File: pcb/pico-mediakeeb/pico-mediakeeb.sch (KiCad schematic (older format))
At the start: 8 parts

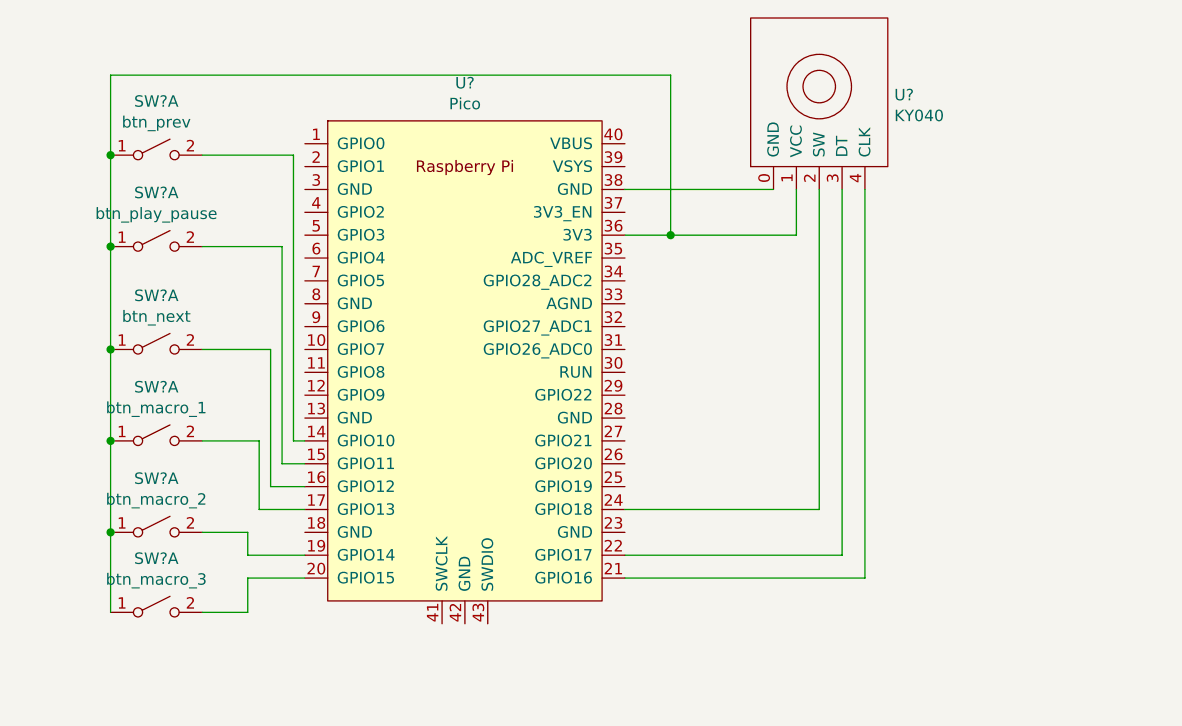
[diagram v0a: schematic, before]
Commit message: Make labels more readable
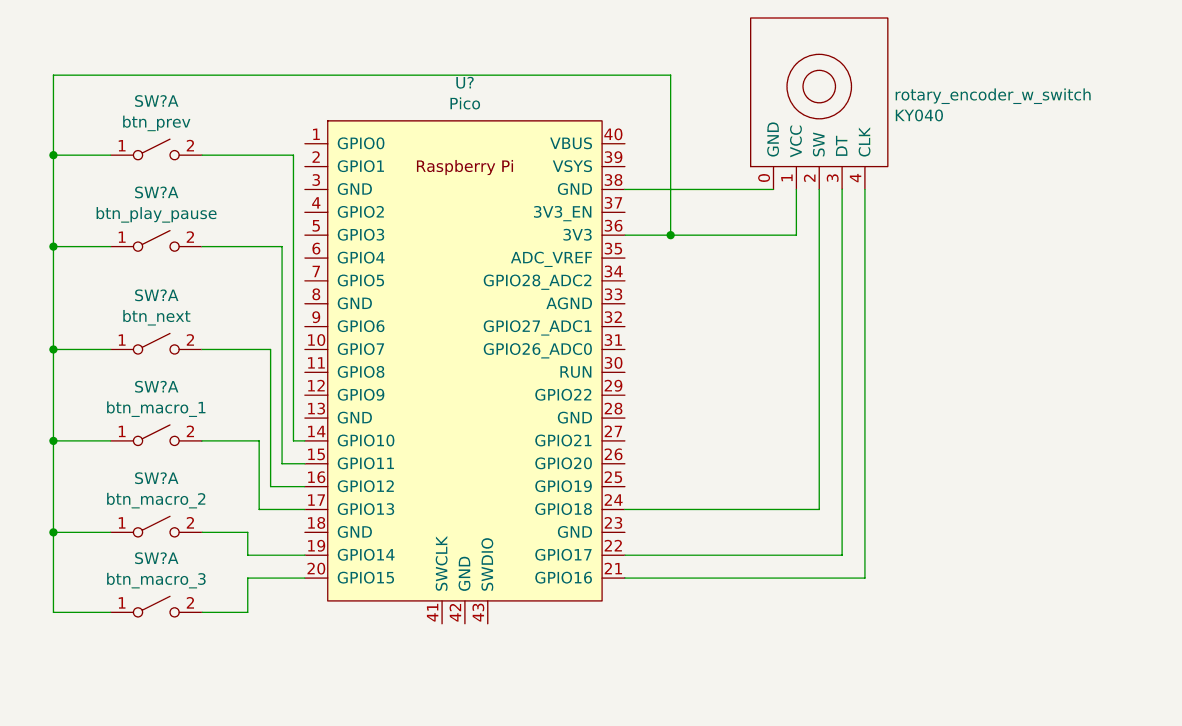
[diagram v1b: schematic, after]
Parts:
- gave numbers to parts that had none: 1
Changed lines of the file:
@@
 	4950 1650 4950 950
-Wire Wire Line
-	4950 950  2500 950
-Wire Wire Line
-	2500 950  2500 1300
-Connection ~ 2500 1300
-Wire Wire Line
-	2500 1300 2500 1700
-Connection ~ 2500 1700
-Wire Wire Line
-	2500 1700 2500 2150
-Connection ~ 2500 2150
-Wire Wire Line
-	2500 2150 2500 2550
-Connection ~ 2500 2550
-Wire Wire Line
-	2500 2550 2500 2950
-Connection ~ 2500 2950
-Wire Wire Line
-	2500 2950 2500 3300
-$Comp
-L pico-mediakeeb:KY040 U?
-U 1 1 6096AC9D
-P 5600 1000
-F 0 "U?" H 5928 963 50  0000 L CNN
-F 1 "KY040" H 5928 872 50  0000 L CNN
-F 2 "" H 5600 1000 50  0001 C CNN
-F 3 "" H 5600 1000 50  0001 C CNN
-	1    5600 1000
-	1    0    0    -1
-$EndComp
 Wire Wire Line
 	4750 1450 5400 1450
@@
 Wire Wire Line
 	5800 3150 4750 3150
+$Comp
+L pico-mediakeeb:KY040 rotary_encoder_w_switch
+U 1 1 6096AC9D
+P 5600 1000
+F 0 "rotary_encoder_w_switch" H 5928 963 50  0000 L CNN
+F 1 "KY040" H 5928 872 50  0000 L CNN
+F 2 "" H 5600 1000 50  0001 C CNN
+F 3 "" H 5600 1000 50  0001 C CNN
+	1    5600 1000
+	1    0    0    -1
+$EndComp
+Wire Wire Line
+	2500 3300 2250 3300
+Wire Wire Line
+	2250 3300 2250 2950
+Wire Wire Line
+	2250 950  4950 950
+Wire Wire Line
+	2500 1300 2250 1300
+Connection ~ 2250 1300
+Wire Wire Line
+	2250 1300 2250 950
+Wire Wire Line
+	2500 1700 2250 1700
+Connection ~ 2250 1700
+Wire Wire Line
+	2250 1700 2250 1300
+Wire Wire Line
+	2500 2150 2250 2150
+Connection ~ 2250 2150
+Wire Wire Line
+	2250 2150 2250 1700
+Wire Wire Line
+	2500 2550 2250 2550
+Connection ~ 2250 2550
+Wire Wire Line
+	2250 2550 2250 2150
+Wire Wire Line
+	2500 2950 2250 2950
+Connection ~ 2250 2950
+Wire Wire Line
+	2250 2950 2250 2550
 $EndSCHEMATC

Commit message: Update schematic to use generic rotary encoder
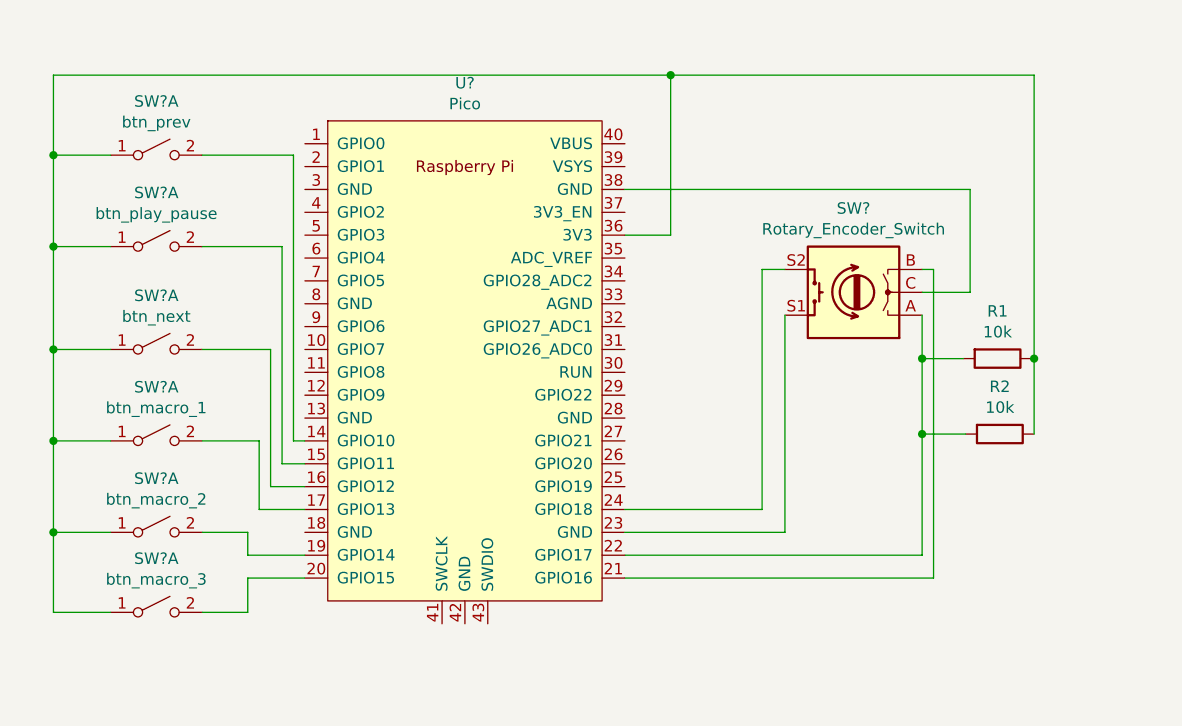
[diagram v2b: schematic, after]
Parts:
- removed rotary_encoder_w_switch: KY040, symbol pico-mediakeeb:KY040
- added R1, R2: 10k, symbol Device:R
- added SW?: Rotary_Encoder_Switch, symbol Device:Rotary_Encoder_Switch
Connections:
- net at U?.21 (GPIO16): now also SW?.B
- net at U?.22 (GPIO17): now also R1.2, R2.2, SW?.A
- net at U?.23 (GND): now also SW?.S1
- net at U?.24 (GPIO18): now also SW?.S2
- net at SW?.1 (A), SW?.1 (A), SW?.1 (A)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: now also R1.1, R2.1
- net at U?.38 (GND): now also SW?.C
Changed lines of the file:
@@
 	4950 1650 4950 950
-Wire Wire Line
-	4750 1450 5400 1450
-Wire Wire Line
-	5500 1450 5500 1650
-Wire Wire Line
-	5500 1650 4950 1650
-Connection ~ 4950 1650
-Wire Wire Line
-	5600 1450 5600 2850
-Wire Wire Line
-	5600 2850 4750 2850
-Wire Wire Line
-	5700 1450 5700 3050
-Wire Wire Line
-	5700 3050 4750 3050
-Wire Wire Line
-	5800 1450 5800 3150
-Wire Wire Line
-	5800 3150 4750 3150
-$Comp
-L pico-mediakeeb:KY040 rotary_encoder_w_switch
-U 1 1 6096AC9D
-P 5600 1000
-F 0 "rotary_encoder_w_switch" H 5928 963 50  0000 L CNN
-F 1 "KY040" H 5928 872 50  0000 L CNN
-F 2 "" H 5600 1000 50  0001 C CNN
-F 3 "" H 5600 1000 50  0001 C CNN
-	1    5600 1000
-	1    0    0    -1
-$EndComp
 Wire Wire Line
 	2500 3300 2250 3300
@@
 Wire Wire Line
 	2250 2950 2250 2550
+$Comp
+L Device:Rotary_Encoder_Switch SW?
+U 1 1 6097F51C
+P 5750 1900
+F 0 "SW?" H 5750 1533 50  0000 C CNN
+F 1 "Rotary_Encoder_Switch" H 5750 1624 50  0000 C CNN
+F 2 "" H 5600 2060 50  0001 C CNN
+F 3 "~" H 5750 2160 50  0001 C CNN
+	1    5750 1900
+	-1   0    0    1
+$EndComp
+Wire Wire Line
+	6050 2000 6050 2190
+Wire Wire Line
+	6050 3050 4750 3050
+Wire Wire Line
+	6050 1800 6100 1800
+Wire Wire Line
+	6100 1800 6100 3150
+Wire Wire Line
+	6100 3150 4750 3150
+Wire Wire Line
+	4750 2950 5450 2950
+Wire Wire Line
+	5450 2950 5450 2000
+Wire Wire Line
+	5450 1800 5350 1800
+Wire Wire Line
+	5350 1800 5350 2850
+Wire Wire Line
+	5350 2850 4750 2850
+Wire Wire Line
+	6050 1900 6260 1900
+Wire Wire Line
+	6260 1900 6260 1450
+Wire Wire Line
+	6260 1450 4750 1450
+$Comp
+L Device:R R1
+U 1 1 6099BEDA
+P 6380 2190
+F 0 "R1" V 6173 2190 50  0000 C CNN
+F 1 "10k" V 6264 2190 50  0000 C CNN
+F 2 "" V 6310 2190 50  0001 C CNN
+F 3 "~" H 6380 2190 50  0001 C CNN
+	1    6380 2190
+	0    1    1    0
+$EndComp
+$Comp
+L Device:R R2
+U 1 1 6099D114
+P 6390 2520
+F 0 "R2" V 6183 2520 50  0000 C CNN
+F 1 "10k" V 6274 2520 50  0000 C CNN
+F 2 "" V 6320 2520 50  0001 C CNN
+F 3 "~" H 6390 2520 50  0001 C CNN
+	1    6390 2520
+	0    1    1    0
+$EndComp
+Wire Wire Line
+	6050 2190 6230 2190
+Connection ~ 6050 2190
+Wire Wire Line
+	6050 2190 6050 2520
+Wire Wire Line
+	6050 2520 6240 2520
+Connection ~ 6050 2520
+Wire Wire Line
+	6050 2520 6050 3050
+Wire Wire Line
+	6540 2520 6540 2190
+Wire Wire Line
+	6540 2190 6530 2190
+Wire Wire Line
+	6540 2190 6540 950
+Wire Wire Line
+	6540 950  4950 950
+Connection ~ 6540 2190
+Connection ~ 4950 950
 $EndSCHEMATC

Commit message: Update schematic
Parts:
- R1, R2: footprint (none) -> Resistor_THT:R_Axial_DIN0204_L3.6mm_D1.6mm_P5.08mm_Vertical
- SW1, SW2, SW3, SW4, SW5, SW6: renamed from SW?; footprint (none) -> Button_Switch_Keyboard:SW_Cherry_MX_1.00u_Plate
- SW7: renamed from SW?; footprint (none) -> Rotary_Encoder:RotaryEncoder_Alps_EC11E-Switch_Vertical_H20mm
- U1: renamed from U?; footprint RPi_Pico:RPi_Pico_SMD_TH -> Raspberry:RPi_Pico_SMD_TH
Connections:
- no-connect marks 0 -> 31
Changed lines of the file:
@@
 $EndDescr
 $Comp
-L MCU_RaspberryPi_and_Boards:Pico U?
+L MCU_RaspberryPi_and_Boards:Pico U1
 U 1 1 609308D7
 P 4050 2200
-F 0 "U?" H 4050 3415 50  0000 C CNN
+F 0 "U1" H 4050 3415 50  0000 C CNN
 F 1 "Pico" H 4050 3324 50  0000 C CNN
-F 2 "RPi_Pico:RPi_Pico_SMD_TH" V 4050 2200 50  0001 C CNN
+F 2 "Raspberry:RPi_Pico_SMD_TH" V 4050 2200 50  0001 C CNN
 F 3 "" H 4050 2200 50  0001 C CNN
 	1    4050 2200
 	1    0    0    -1
 $EndComp
-$Comp
-L Switch:SW_DPST_x2 SW?
-U 1 1 60931FB6
-P 2700 1300
-F 0 "SW?" H 2700 1535 50  0000 C CNN
-F 1 "btn_prev" H 2700 1444 50  0000 C CNN
-F 2 "" H 2700 1300 50  0001 C CNN
-F 3 "~" H 2700 1300 50  0001 C CNN
-	1    2700 1300
-	1    0    0    -1
-$EndComp
-$Comp
-L Switch:SW_DPST_x2 SW?
-U 1 1 6093271C
-P 2700 1700
-F 0 "SW?" H 2700 1935 50  0000 C CNN
-F 1 "btn_play_pause" H 2700 1844 50  0000 C CNN
-F 2 "" H 2700 1700 50  0001 C CNN
-F 3 "~" H 2700 1700 50  0001 C CNN
-	1    2700 1700
-	1    0    0    -1
-$EndComp
-$Comp
-L Switch:SW_DPST_x2 SW?
-U 1 1 609327D9
-P 2700 2150
-F 0 "SW?" H 2700 2385 50  0000 C CNN
-F 1 "btn_next" H 2700 2294 50  0000 C CNN
-F 2 "" H 2700 2150 50  0001 C CNN
-F 3 "~" H 2700 2150 50  0001 C CNN
-	1    2700 2150
-	1    0    0    -1
-$EndComp
-$Comp
-L Switch:SW_DPST_x2 SW?
-U 1 1 60940915
-P 2700 2550
-F 0 "SW?" H 2700 2785 50  0000 C CNN
-F 1 "btn_macro_1" H 2700 2694 50  0000 C CNN
-F 2 "" H 2700 2550 50  0001 C CNN
-F 3 "~" H 2700 2550 50  0001 C CNN
-	1    2700 2550
-	1    0    0    -1
-$EndComp
-$Comp
-L Switch:SW_DPST_x2 SW?
-U 1 1 6094091B
-P 2700 2950
-F 0 "SW?" H 2700 3185 50  0000 C CNN
-F 1 "btn_macro_2" H 2700 3094 50  0000 C CNN
-F 2 "" H 2700 2950 50  0001 C CNN
-F 3 "~" H 2700 2950 50  0001 C CNN
-	1    2700 2950
-	1    0    0    -1
-$EndComp
-$Comp
-L Switch:SW_DPST_x2 SW?
-U 1 1 60940921
-P 2700 3300
-F 0 "SW?" H 2700 3535 50  0000 C CNN
-F 1 "btn_macro_3" H 2700 3444 50  0000 C CNN
-F 2 "" H 2700 3300 50  0001 C CNN
-F 3 "~" H 2700 3300 50  0001 C CNN
-	1    2700 3300
-	1    0    0    -1
-$EndComp
 Wire Wire Line
 	3300 1300 3300 2550
@@
 	3300 2550 3350 2550
 Wire Wire Line
-	2900 1300 3300 1300
-Wire Wire Line
-	2900 1700 3250 1700
-Wire Wire Line
 	3250 1700 3250 2650
 Wire Wire Line
 	3250 2650 3350 2650
 Wire Wire Line
-	2900 2150 3200 2150
-Wire Wire Line
 	3200 2150 3200 2750
 Wire Wire Line
 	3200 2750 3350 2750
 Wire Wire Line
-	2900 2550 3150 2550
-Wire Wire Line
 	3150 2550 3150 2850
 Wire Wire Line
 	3150 2850 3350 2850
 Wire Wire Line
-	2900 2950 3100 2950
-Wire Wire Line
 	3100 2950 3100 3050
 Wire Wire Line
 	3100 3050 3350 3050
-Wire Wire Line
-	2900 3300 3100 3300
 Wire Wire Line
 	3100 3300 3100 3150
@@
 	2250 2950 2250 2550
 $Comp
-L Device:Rotary_Encoder_Switch SW?
+L Device:Rotary_Encoder_Switch SW7
 U 1 1 6097F51C
 P 5750 1900
-F 0 "SW?" H 5750 1533 50  0000 C CNN
+F 0 "SW7" H 5750 1533 50  0000 C CNN
 F 1 "Rotary_Encoder_Switch" H 5750 1624 50  0000 C CNN
-F 2 "" H 5600 2060 50  0001 C CNN
+F 2 "Rotary_Encoder:RotaryEncoder_Alps_EC11E-Switch_Vertical_H20mm" H 5600 2060 50  0001 C CNN
 F 3 "~" H 5750 2160 50  0001 C CNN
 	1    5750 1900
@@
 Wire Wire Line
 	6100 3150 4750 3150
-Wire Wire Line
-	4750 2950 5450 2950
-Wire Wire Line
-	5450 2950 5450 2000
 Wire Wire Line
 	5450 1800 5350 1800
@@
 F 0 "R1" V 6173 2190 50  0000 C CNN
 F 1 "10k" V 6264 2190 50  0000 C CNN
-F 2 "" V 6310 2190 50  0001 C CNN
+F 2 "Resistor_THT:R_Axial_DIN0204_L3.6mm_D1.6mm_P5.08mm_Vertical" V 6310 2190 50  0001 C CNN
 F 3 "~" H 6380 2190 50  0001 C CNN
 	1    6380 2190
@@
 F 0 "R2" V 6183 2520 50  0000 C CNN
 F 1 "10k" V 6274 2520 50  0000 C CNN
-F 2 "" V 6320 2520 50  0001 C CNN
+F 2 "Resistor_THT:R_Axial_DIN0204_L3.6mm_D1.6mm_P5.08mm_Vertical" V 6320 2520 50  0001 C CNN
 F 3 "~" H 6390 2520 50  0001 C CNN
 	1    6390 2520
@@
 Connection ~ 6540 2190
 Connection ~ 4950 950
+NoConn ~ 4750 2050
+NoConn ~ 4750 1950
+NoConn ~ 4750 1850
+NoConn ~ 4750 1750
+NoConn ~ 4750 2750
+NoConn ~ 4750 2650
+NoConn ~ 4750 2550
+NoConn ~ 4750 2450
+NoConn ~ 4750 2350
+NoConn ~ 4750 2250
+NoConn ~ 4750 2150
+NoConn ~ 4750 1350
+NoConn ~ 4750 1250
+NoConn ~ 4750 1550
+NoConn ~ 3350 2950
+NoConn ~ 3350 2450
+NoConn ~ 3350 2350
+NoConn ~ 3350 2250
+NoConn ~ 3350 2150
+NoConn ~ 3350 2050
+NoConn ~ 3350 1950
+NoConn ~ 3350 1250
+NoConn ~ 3350 1350
+NoConn ~ 3350 1450
+NoConn ~ 3350 1550
+NoConn ~ 3350 1650
+NoConn ~ 3350 1750
+NoConn ~ 3350 1850
+NoConn ~ 3950 3350
+NoConn ~ 4050 3350
+NoConn ~ 4150 3350
+Wire Wire Line
+	5450 2950 5450 2000
+Wire Wire Line
+	4750 2950 5450 2950
+Wire Wire Line
+	2900 3300 3100 3300
+Wire Wire Line
+	2900 2950 3100 2950
+Wire Wire Line
+	2900 2550 3150 2550
+Wire Wire Line
+	2900 2150 3200 2150
+Wire Wire Line
+	2900 1700 3250 1700
+Wire Wire Line
+	2900 1300 3300 1300
+$Comp
+L Switch:SW_DPST_x2 SW6
+U 1 1 60940921
+P 2700 3300
+F 0 "SW6" H 2700 3535 50  0000 C CNN
+F 1 "btn_macro_3" H 2700 3444 50  0000 C CNN
+F 2 "Button_Switch_Keyboard:SW_Cherry_MX_1.00u_Plate" H 2700 3300 50  0001 C CNN
+F 3 "~" H 2700 3300 50  0001 C CNN
+	1    2700 3300
+	1    0    0    -1
+$EndComp
+$Comp
+L Switch:SW_DPST_x2 SW5
+U 1 1 6094091B
+P 2700 2950
+F 0 "SW5" H 2700 3185 50  0000 C CNN
+F 1 "btn_macro_2" H 2700 3094 50  0000 C CNN
+F 2 "Button_Switch_Keyboard:SW_Cherry_MX_1.00u_Plate" H 2700 2950 50  0001 C CNN
+F 3 "~" H 2700 2950 50  0001 C CNN
+	1    2700 2950
+	1    0    0    -1
+$EndComp
+$Comp
+L Switch:SW_DPST_x2 SW4
+U 1 1 60940915
+P 2700 2550
+F 0 "SW4" H 2700 2785 50  0000 C CNN
+F 1 "btn_macro_1" H 2700 2694 50  0000 C CNN
+F 2 "Button_Switch_Keyboard:SW_Cherry_MX_1.00u_Plate" H 2700 2550 50  0001 C CNN
+F 3 "~" H 2700 2550 50  0001 C CNN
+	1    2700 2550
+	1    0    0    -1
+$EndComp
+$Comp
+L Switch:SW_DPST_x2 SW3
+U 1 1 609327D9
+P 2700 2150
+F 0 "SW3" H 2700 2385 50  0000 C CNN
+F 1 "btn_next" H 2700 2294 50  0000 C CNN
+F 2 "Button_Switch_Keyboard:SW_Cherry_MX_1.00u_Plate" H 2700 2150 50  0001 C CNN
+F 3 "~" H 2700 2150 50  0001 C CNN
+	1    2700 2150
+	1    0    0    -1
+$EndComp
+$Comp
+L Switch:SW_DPST_x2 SW2
+U 1 1 6093271C
+P 2700 1700
+F 0 "SW2" H 2700 1935 50  0000 C CNN
+F 1 "btn_play_pause" H 2700 1844 50  0000 C CNN
+F 2 "Button_Switch_Keyboard:SW_Cherry_MX_1.00u_Plate" H 2700 1700 50  0001 C CNN
+F 3 "~" H 2700 1700 50  0001 C CNN
+	1    2700 1700
+	1    0    0    -1
+$EndComp
+$Comp
+L Switch:SW_DPST_x2 SW1
+U 1 1 60931FB6
+P 2700 1300
+F 0 "SW1" H 2700 1535 50  0000 C CNN
+F 1 "btn_prev" H 2700 1444 50  0000 C CNN
+F 2 "Button_Switch_Keyboard:SW_Cherry_MX_1.00u_Plate" H 2700 1300 50  0001 C CNN
+F 3 "~" H 2700 1300 50  0001 C CNN
+	1    2700 1300
+	1    0    0    -1
+$EndComp
 $EndSCHEMATC

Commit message: Update schematic
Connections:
- net labels added: +3.3V, GND
- wire segments 54 -> 50
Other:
- moved on the sheet: R1, R2
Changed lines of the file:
@@
 Wire Wire Line
 	3100 3150 3350 3150
-Wire Wire Line
-	4750 1650 4950 1650
-Wire Wire Line
-	4950 1650 4950 950
-Wire Wire Line
-	2500 3300 2250 3300
-Wire Wire Line
-	2250 3300 2250 2950
-Wire Wire Line
-	2250 950  4950 950
-Wire Wire Line
-	2500 1300 2250 1300
-Connection ~ 2250 1300
-Wire Wire Line
-	2250 1300 2250 950
-Wire Wire Line
-	2500 1700 2250 1700
-Connection ~ 2250 1700
-Wire Wire Line
-	2250 1700 2250 1300
-Wire Wire Line
-	2500 2150 2250 2150
-Connection ~ 2250 2150
-Wire Wire Line
-	2250 2150 2250 1700
-Wire Wire Line
-	2500 2550 2250 2550
-Connection ~ 2250 2550
-Wire Wire Line
-	2250 2550 2250 2150
-Wire Wire Line
-	2500 2950 2250 2950
-Connection ~ 2250 2950
-Wire Wire Line
-	2250 2950 2250 2550
 $Comp
 L Device:Rotary_Encoder_Switch SW7
@@
 $EndComp
 Wire Wire Line
-	6050 2000 6050 2190
-Wire Wire Line
 	6050 3050 4750 3050
 Wire Wire Line
-	6050 1800 6100 1800
-Wire Wire Line
-	6100 1800 6100 3150
-Wire Wire Line
-	6100 3150 4750 3150
-Wire Wire Line
 	5450 1800 5350 1800
 Wire Wire Line
@@
 Wire Wire Line
 	5350 2850 4750 2850
-Wire Wire Line
-	6050 1900 6260 1900
-Wire Wire Line
-	6260 1900 6260 1450
-Wire Wire Line
-	6260 1450 4750 1450
-$Comp
-L Device:R R1
-U 1 1 6099BEDA
-P 6380 2190
-F 0 "R1" V 6173 2190 50  0000 C CNN
-F 1 "10k" V 6264 2190 50  0000 C CNN
-F 2 "Resistor_THT:R_Axial_DIN0204_L3.6mm_D1.6mm_P5.08mm_Vertical" V 6310 2190 50  0001 C CNN
-F 3 "~" H 6380 2190 50  0001 C CNN
-	1    6380 2190
-	0    1    1    0
-$EndComp
-$Comp
-L Device:R R2
-U 1 1 6099D114
-P 6390 2520
-F 0 "R2" V 6183 2520 50  0000 C CNN
-F 1 "10k" V 6274 2520 50  0000 C CNN
-F 2 "Resistor_THT:R_Axial_DIN0204_L3.6mm_D1.6mm_P5.08mm_Vertical" V 6320 2520 50  0001 C CNN
-F 3 "~" H 6390 2520 50  0001 C CNN
-	1    6390 2520
-	0    1    1    0
-$EndComp
-Wire Wire Line
-	6050 2190 6230 2190
-Connection ~ 6050 2190
-Wire Wire Line
-	6050 2190 6050 2520
-Wire Wire Line
-	6050 2520 6240 2520
-Connection ~ 6050 2520
-Wire Wire Line
-	6050 2520 6050 3050
-Wire Wire Line
-	6540 2520 6540 2190
-Wire Wire Line
-	6540 2190 6530 2190
-Wire Wire Line
-	6540 2190 6540 950
-Wire Wire Line
-	6540 950  4950 950
-Connection ~ 6540 2190
-Connection ~ 4950 950
 NoConn ~ 4750 2050
 NoConn ~ 4750 1950
@@
 	1    0    0    -1
 $EndComp
+$Comp
+L power:+3.3V #PWR?
+U 1 1 60945260
+P 2250 3490
+F 0 "#PWR?" H 2250 3340 50  0001 C CNN
+F 1 "+3.3V" H 2265 3663 50  0000 C CNN
+F 2 "" H 2250 3490 50  0001 C CNN
+F 3 "" H 2250 3490 50  0001 C CNN
+	1    2250 3490
+	-1   0    0    1
+$EndComp
+$Comp
+L power:+3.3V #PWR?
+U 1 1 60946472
+P 6580 2650
+F 0 "#PWR?" H 6580 2500 50  0001 C CNN
+F 1 "+3.3V" H 6595 2823 50  0000 C CNN
+F 2 "" H 6580 2650 50  0001 C CNN
+F 3 "" H 6580 2650 50  0001 C CNN
+	1    6580 2650
+	-1   0    0    1
+$EndComp
+$Comp
+L power:+3.3V #PWR?
+U 1 1 6094B363
+P 4750 1650
+F 0 "#PWR?" H 4750 1500 50  0001 C CNN
+F 1 "+3.3V" H 4765 1823 50  0000 C CNN
+F 2 "" H 4750 1650 50  0001 C CNN
+F 3 "" H 4750 1650 50  0001 C CNN
+	1    4750 1650
+	0    1    1    0
+$EndComp
+$Comp
+L Device:R R1
+U 1 1 6099BEDA
+P 6930 2410
+F 0 "R1" V 6723 2410 50  0000 C CNN
+F 1 "10k" V 6814 2410 50  0000 C CNN
+F 2 "Resistor_THT:R_Axial_DIN0204_L3.6mm_D1.6mm_P5.08mm_Vertical" V 6860 2410 50  0001 C CNN
+F 3 "~" H 6930 2410 50  0001 C CNN
+	1    6930 2410
+	0    1    1    0
+$EndComp
+$Comp
+L Device:R R2
+U 1 1 6099D114
+P 6200 2250
+F 0 "R2" V 5993 2250 50  0000 C CNN
+F 1 "10k" V 6084 2250 50  0000 C CNN
+F 2 "Resistor_THT:R_Axial_DIN0204_L3.6mm_D1.6mm_P5.08mm_Vertical" V 6130 2250 50  0001 C CNN
+F 3 "~" H 6200 2250 50  0001 C CNN
+	1    6200 2250
+	0    1    1    0
+$EndComp
+Wire Wire Line
+	7090 2410 7080 2410
+Wire Wire Line
+	6050 2000 6050 2250
+$Comp
+L power:GND #PWR?
+U 1 1 609660FD
+P 6050 1900
+F 0 "#PWR?" H 6050 1650 50  0001 C CNN
+F 1 "GND" H 6055 1727 50  0000 C CNN
+F 2 "" H 6050 1900 50  0001 C CNN
+F 3 "" H 6050 1900 50  0001 C CNN
+	1    6050 1900
+	0    -1   -1   0
+$EndComp
+Wire Wire Line
+	7090 1800 7090 2410
+Wire Wire Line
+	6050 1800 7090 1800
+Wire Wire Line
+	4750 3150 7090 3150
+Connection ~ 6050 2250
+Wire Wire Line
+	6050 2250 6050 3050
+Connection ~ 7090 2410
+Wire Wire Line
+	7090 2410 7090 3150
+Wire Wire Line
+	6580 2250 6580 2410
+Wire Wire Line
+	6350 2250 6580 2250
+Wire Wire Line
+	6580 2410 6780 2410
+Connection ~ 6580 2410
+Wire Wire Line
+	6580 2410 6580 2650
+Connection ~ 6780 2410
+Wire Wire Line
+	6780 2410 6790 2410
+Wire Wire Line
+	2500 1300 2250 1300
+Wire Wire Line
+	2500 3300 2250 3300
+Connection ~ 2250 3300
+Wire Wire Line
+	2250 3300 2250 3490
+Wire Wire Line
+	2500 2950 2250 2950
+Connection ~ 2250 2950
+Wire Wire Line
+	2250 2950 2250 3300
+Wire Wire Line
+	2500 2550 2250 2550
+Connection ~ 2250 2550
+Wire Wire Line
+	2250 2550 2250 2950
+Wire Wire Line
+	2510 2150 2500 2150
+Connection ~ 2250 2150
+Wire Wire Line
+	2250 2150 2250 2550
+Connection ~ 2500 2150
+Wire Wire Line
+	2500 2150 2250 2150
+Wire Wire Line
+	2510 1700 2500 1700
+Wire Wire Line
+	2250 1300 2250 1700
+Connection ~ 2250 1700
+Wire Wire Line
+	2250 1700 2250 2150
+Connection ~ 2500 1700
+Wire Wire Line
+	2500 1700 2250 1700
+$Comp
+L power:GND #PWR?
+U 1 1 60947068
+P 4750 1450
+F 0 "#PWR?" H 4750 1200 50  0001 C CNN
+F 1 "GND" H 4755 1277 50  0000 C CNN
+F 2 "" H 4750 1450 50  0001 C CNN
+F 3 "" H 4750 1450 50  0001 C CNN
+	1    4750 1450
+	0    -1   -1   0
+$EndComp
 $EndSCHEMATC
